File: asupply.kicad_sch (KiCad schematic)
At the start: 108 parts, among them U10 LT3081xDF, U11 LT3042xMSE, U12 LT3045xMSE, U13 LT3045xMSE, U14 LT3042xMSE, U15 LT3094xMSE, U16 LT3042xMSE, U9 LTC3261

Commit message: change diodes
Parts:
- gave numbers to parts that had none: 1
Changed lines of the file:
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@@
   (symbol (lib_id "Device:C") (at 226.06 119.38 0) (unit 1)
     (in_bom yes) (on_board yes)
-    (property "Reference" "C?" (id 0) (at 229.87 121.92 0)
+    (property "Reference" "C193" (id 0) (at 229.87 121.92 0)
       (effects (font (size 1.27 1.27)) (justify left))
     )

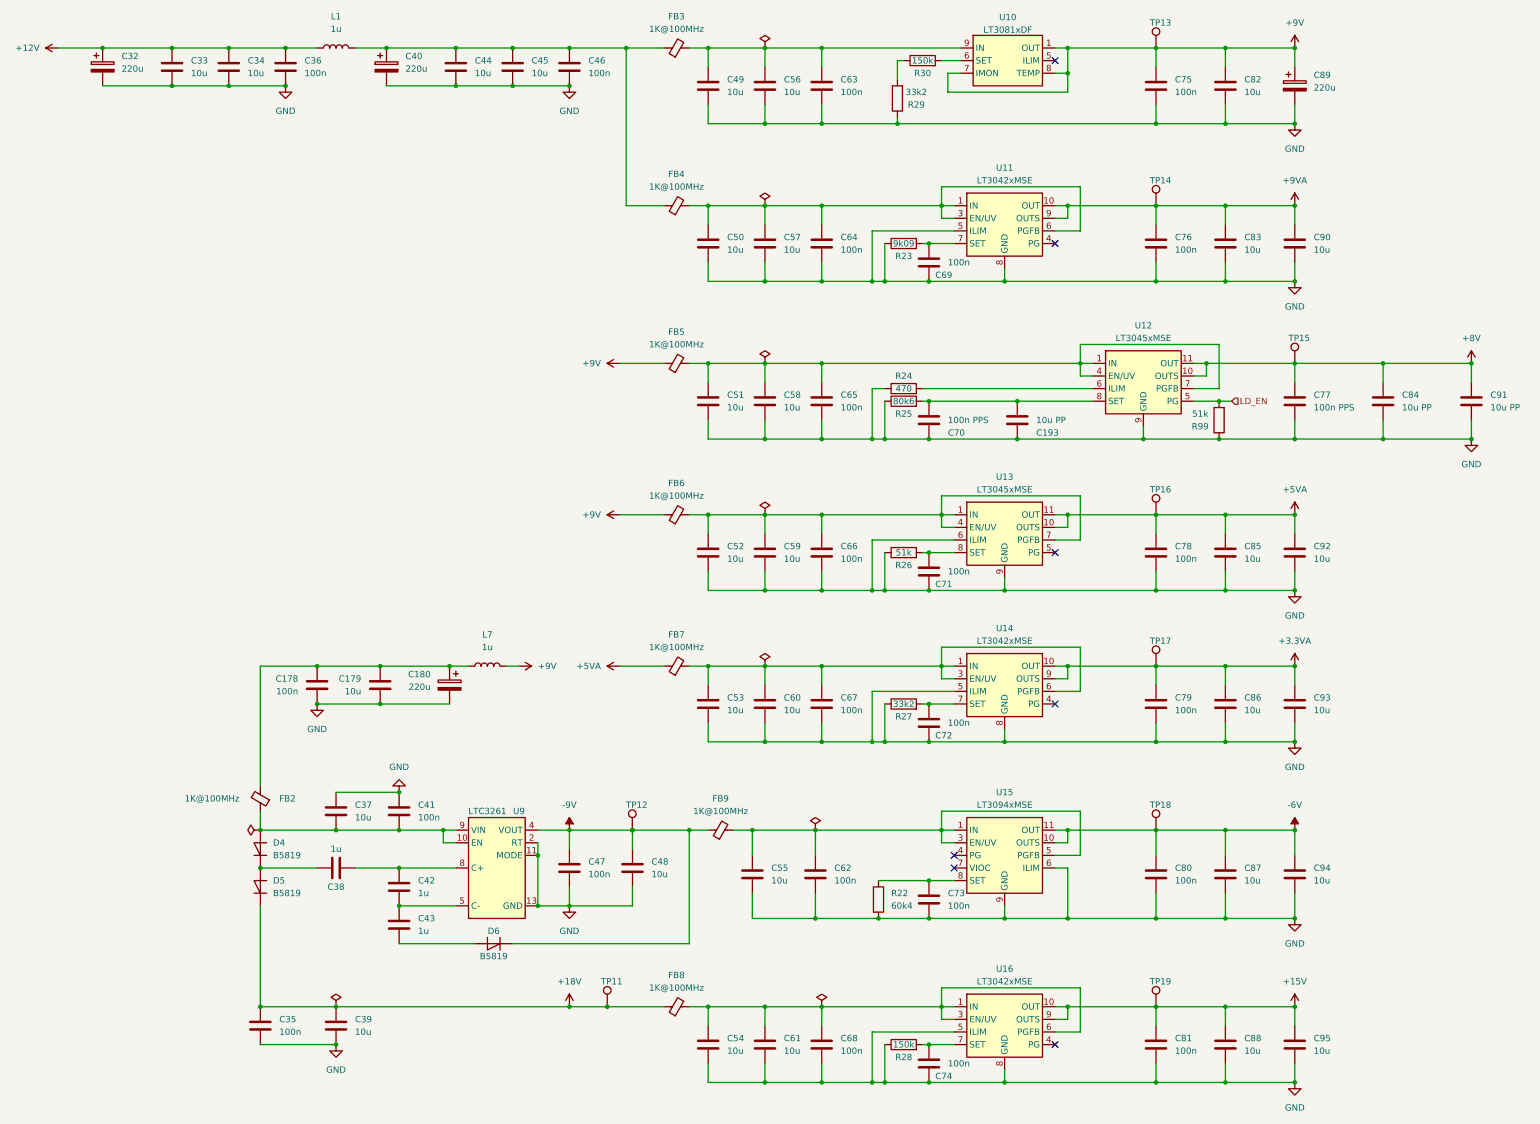
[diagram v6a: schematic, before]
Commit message: import sch to pcb
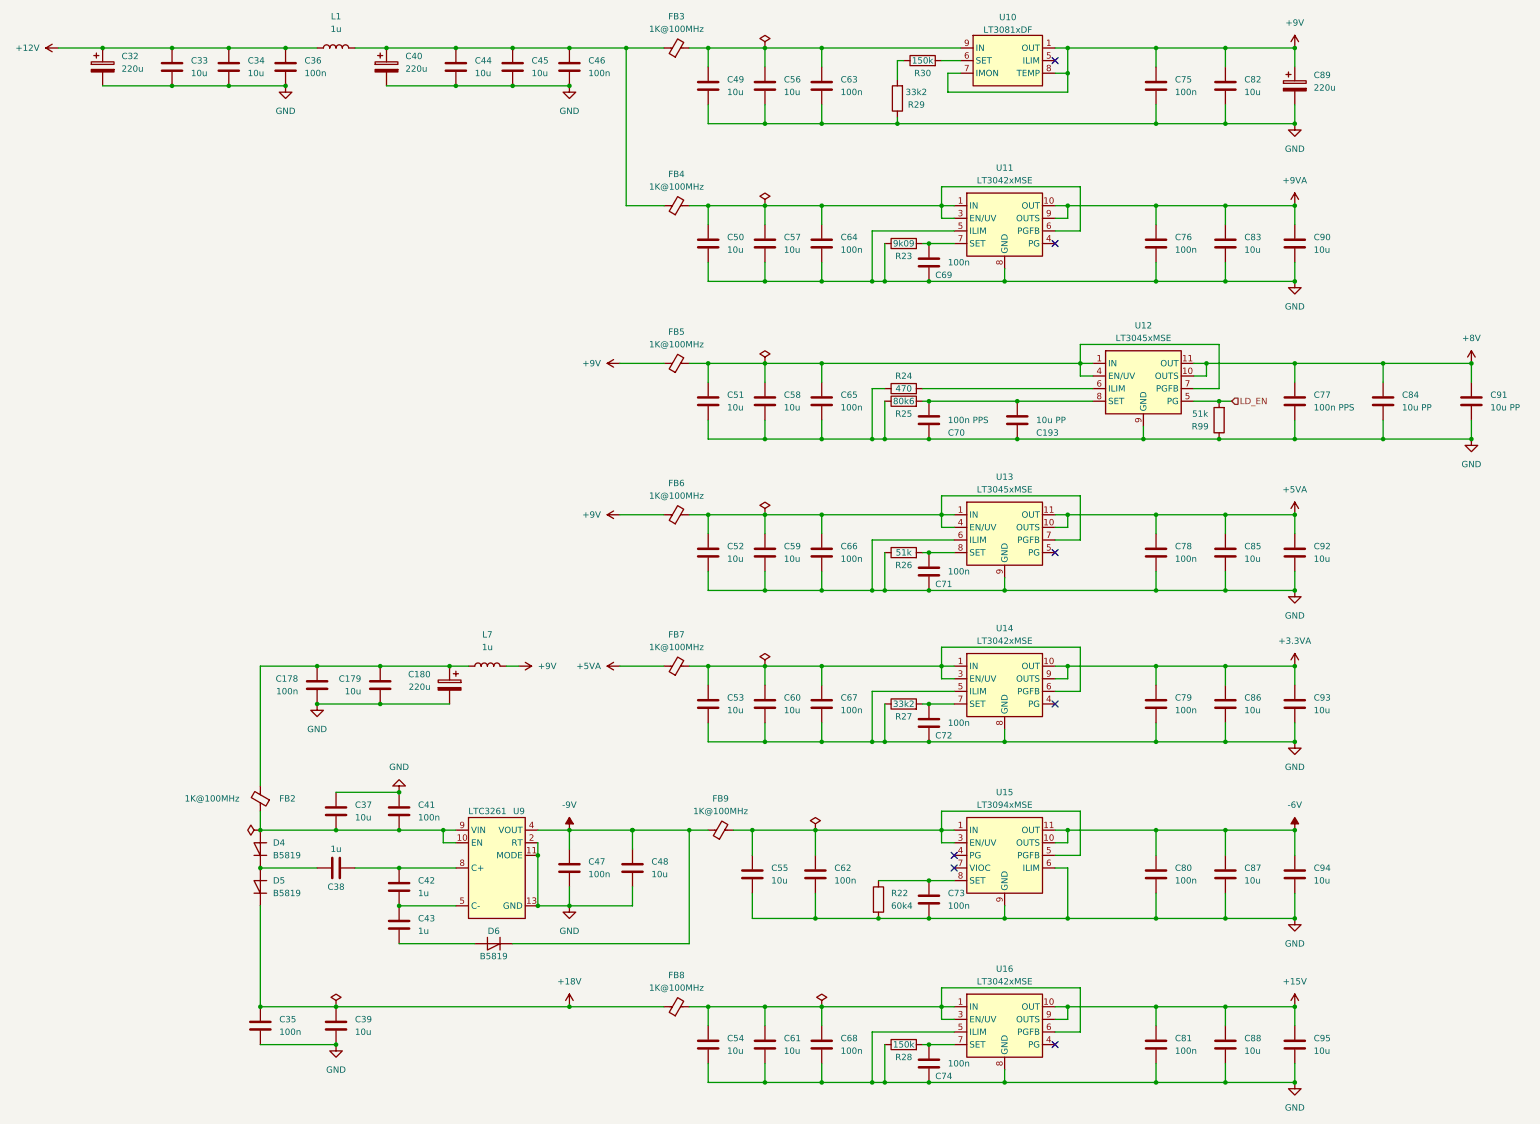
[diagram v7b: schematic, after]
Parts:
- removed TP11, TP12, TP13, TP14, TP15, TP16, TP17, TP18, TP19: TestPoint, TestPoint:TestPoint_Pad_2.0x2.0mm, symbol Connector:TestPoint
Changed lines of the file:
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@@
   (junction (at 254 91.44) (diameter 0) (color 0 0 0 0)
   )
-  (junction (at 143.51 237.49) (diameter 0) (color 0 0 0 0)
-  )
   (junction (at 135.89 237.49) (diameter 0) (color 0 0 0 0)
   )
@@
     (stroke (width 0) (type default) (color 0 0 0 0))
   )
-  (wire (pts (xy 135.89 237.49) (xy 143.51 237.49))
+  (wire (pts (xy 135.89 237.49) (xy 154.94 237.49))
     (stroke (width 0) (type default) (color 0 0 0 0))
   )
@@
     (stroke (width 0) (type default) (color 0 0 0 0))
   )
-  (wire (pts (xy 143.51 237.49) (xy 154.94 237.49))
-    (stroke (width 0) (type default) (color 0 0 0 0))
-  )
   (wire (pts (xy 199.39 91.44) (xy 208.28 91.44))
     (stroke (width 0) (type default) (color 0 0 0 0))
@@
     (pin "2")
   )
-  (symbol (lib_id "Connector:TestPoint") (at 281.94 107.95 0) (unit 1)
-    (in_bom yes) (on_board yes)
-    (property "Reference" "TP15" (id 0) (at 280.67 102.87 0)
-      (effects (font (size 1.27 1.27)) (justify left))
-    )
-    (property "Value" "TestPoint" (id 1) (at 283.337 106.3502 0)
-      (effects (font (size 1.27 1.27)) (justify left) hide)
-    )
-    (property "Footprint" "TestPoint:TestPoint_Pad_2.0x2.0mm" (id 2) (at 287.02 107.95 0)
-      (effects (font (size 1.27 1.27)) hide)
-    )
-    (property "Datasheet" "~" (id 3) (at 287.02 107.95 0)
-      (effects (font (size 1.27 1.27)) hide)
-    )
-    (pin "1")
-  )
   (symbol (lib_id "power:-9V") (at 135.89 201.93 0) (unit 1)
     (in_bom yes) (on_board yes) (fields_autoplaced)
@@
     (pin "2")
   )
-  (symbol (lib_id "Connector:TestPoint") (at 254 168.91 0) (unit 1)
-    (in_bom yes) (on_board yes)
-    (property "Reference" "TP17" (id 0) (at 252.73 163.83 0)
-      (effects (font (size 1.27 1.27)) (justify left))
-    )
-    (property "Value" "TestPoint" (id 1) (at 255.397 167.3102 0)
-      (effects (font (size 1.27 1.27)) (justify left) hide)
-    )
-    (property "Footprint" "TestPoint:TestPoint_Pad_2.0x2.0mm" (id 2) (at 259.08 168.91 0)
-      (effects (font (size 1.27 1.27)) hide)
-    )
-    (property "Datasheet" "~" (id 3) (at 259.08 168.91 0)
-      (effects (font (size 1.27 1.27)) hide)
-    )
-    (pin "1")
-  )
   (symbol (lib_id "Device:C") (at 208.28 119.38 0) (unit 1)
     (in_bom yes) (on_board yes)
@@
     (pin "2")
   )
-  (symbol (lib_id "Connector:TestPoint") (at 254 138.43 0) (unit 1)
-    (in_bom yes) (on_board yes)
-    (property "Reference" "TP16" (id 0) (at 252.73 133.35 0)
-      (effects (font (size 1.27 1.27)) (justify left))
-    )
-    (property "Value" "TestPoint" (id 1) (at 255.397 136.8302 0)
-      (effects (font (size 1.27 1.27)) (justify left) hide)
-    )
-    (property "Footprint" "TestPoint:TestPoint_Pad_2.0x2.0mm" (id 2) (at 259.08 138.43 0)
-      (effects (font (size 1.27 1.27)) hide)
-    )
-    (property "Datasheet" "~" (id 3) (at 259.08 138.43 0)
-      (effects (font (size 1.27 1.27)) hide)
-    )
-    (pin "1")
-  )
   (symbol (lib_id "Device:C") (at 281.94 115.57 0) (unit 1)
     (in_bom yes) (on_board yes) (fields_autoplaced)
@@
     (pin "1")
   )
-  (symbol (lib_id "Connector:TestPoint") (at 254 201.93 0) (unit 1)
-    (in_bom yes) (on_board yes)
-    (property "Reference" "TP18" (id 0) (at 252.73 196.85 0)
-      (effects (font (size 1.27 1.27)) (justify left))
-    )
-    (property "Value" "TestPoint" (id 1) (at 255.397 200.3302 0)
-      (effects (font (size 1.27 1.27)) (justify left) hide)
-    )
-    (property "Footprint" "TestPoint:TestPoint_Pad_2.0x2.0mm" (id 2) (at 259.08 201.93 0)
-      (effects (font (size 1.27 1.27)) hide)
-    )
-    (property "Datasheet" "~" (id 3) (at 259.08 201.93 0)
-      (effects (font (size 1.27 1.27)) hide)
-    )
-    (pin "1")
-  )
-  (symbol (lib_id "Connector:TestPoint") (at 254 237.49 0) (unit 1)
-    (in_bom yes) (on_board yes)
-    (property "Reference" "TP19" (id 0) (at 252.73 232.41 0)
-      (effects (font (size 1.27 1.27)) (justify left))
-    )
-    (property "Value" "TestPoint" (id 1) (at 255.397 235.8902 0)
-      (effects (font (size 1.27 1.27)) (justify left) hide)
-    )
-    (property "Footprint" "TestPoint:TestPoint_Pad_2.0x2.0mm" (id 2) (at 259.08 237.49 0)
-      (effects (font (size 1.27 1.27)) hide)
-    )
-    (property "Datasheet" "~" (id 3) (at 259.08 237.49 0)
-      (effects (font (size 1.27 1.27)) hide)
-    )
-    (pin "1")
-  )
   (symbol (lib_id "power:PWR_FLAG") (at 73.66 201.93 90) (unit 1)
     (in_bom yes) (on_board yes) (fields_autoplaced)
@@
     (pin "1")
   )
-  (symbol (lib_id "Connector:TestPoint") (at 148.556 201.93 0) (unit 1)
-    (in_bom yes) (on_board yes)
-    (property "Reference" "TP12" (id 0) (at 147.286 196.85 0)
-      (effects (font (size 1.27 1.27)) (justify left))
-    )
-    (property "Value" "TestPoint" (id 1) (at 149.953 200.3302 0)
-      (effects (font (size 1.27 1.27)) (justify left) hide)
-    )
-    (property "Footprint" "TestPoint:TestPoint_Pad_2.0x2.0mm" (id 2) (at 153.636 201.93 0)
-      (effects (font (size 1.27 1.27)) hide)
-    )
-    (property "Datasheet" "~" (id 3) (at 153.636 201.93 0)
-      (effects (font (size 1.27 1.27)) hide)
-    )
-    (pin "1")
-  )
   (symbol (lib_id "Device:C") (at 267.97 245.11 0) (unit 1)
     (in_bom yes) (on_board yes) (fields_autoplaced)
@@
     (pin "1")
   )
-  (symbol (lib_id "Connector:TestPoint") (at 254 44.45 0) (unit 1)
-    (in_bom yes) (on_board yes)
-    (property "Reference" "TP13" (id 0) (at 252.73 39.37 0)
-      (effects (font (size 1.27 1.27)) (justify left))
-    )
-    (property "Value" "TestPoint" (id 1) (at 255.397 42.8502 0)
-      (effects (font (size 1.27 1.27)) (justify left) hide)
-    )
-    (property "Footprint" "TestPoint:TestPoint_Pad_2.0x2.0mm" (id 2) (at 259.08 44.45 0)
-      (effects (font (size 1.27 1.27)) hide)
-    )
-    (property "Datasheet" "~" (id 3) (at 259.08 44.45 0)
-      (effects (font (size 1.27 1.27)) hide)
-    )
-    (pin "1")
-  )
   (symbol (lib_id "Device:D_Shockley") (at 120.65 224.79 180) (unit 1)
     (in_bom yes) (on_board yes)
@@
     (pin "2")
   )
-  (symbol (lib_id "Connector:TestPoint") (at 254 76.2 0) (unit 1)
-    (in_bom yes) (on_board yes)
-    (property "Reference" "TP14" (id 0) (at 252.73 71.12 0)
-      (effects (font (size 1.27 1.27)) (justify left))
-    )
-    (property "Value" "TestPoint" (id 1) (at 255.397 74.6002 0)
-      (effects (font (size 1.27 1.27)) (justify left) hide)
-    )
-    (property "Footprint" "TestPoint:TestPoint_Pad_2.0x2.0mm" (id 2) (at 259.08 76.2 0)
-      (effects (font (size 1.27 1.27)) hide)
-    )
-    (property "Datasheet" "~" (id 3) (at 259.08 76.2 0)
-      (effects (font (size 1.27 1.27)) hide)
-    )
-    (pin "1")
-  )
   (symbol (lib_id "Device:C") (at 135.89 209.55 0) (unit 1)
     (in_bom yes) (on_board yes) (fields_autoplaced)
@@
       (effects (font (size 1.27 1.27)) hide)
     )
-    (pin "1")
-  )
-  (symbol (lib_id "Connector:TestPoint") (at 143.51 237.49 0) (unit 1)
-    (in_bom yes) (on_board yes)
-    (property "Reference" "TP11" (id 0) (at 142.24 232.41 0)
-      (effects (font (size 1.27 1.27)) (justify left))
-    )
-    (property "Value" "TestPoint" (id 1) (at 144.907 235.8902 0)
-      (effects (font (size 1.27 1.27)) (justify left) hide)
-    )
-    (property "Footprint" "TestPoint:TestPoint_Pad_2.0x2.0mm" (id 2) (at 148.59 237.49 0)
-      (effects (font (size 1.27 1.27)) hide)
-    )
-    (property "Datasheet" "~" (id 3) (at 148.59 237.49 0)
-      (effects (font (size 1.27 1.27)) hide)
-    )

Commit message: sync
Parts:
- removed C193: 10u PP, Capacitor_SMD:C_1812_4532Metric, symbol Device:C
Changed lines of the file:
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@@
   (junction (at 186.69 76.2) (diameter 0) (color 0 0 0 0)
   )
-  (junction (at 226.06 123.19) (diameter 0) (color 0 0 0 0)
-  )
   (junction (at 198.12 219.71) (diameter 0) (color 0 0 0 0)
   )
@@
   (junction (at 88.9 201.93) (diameter 0) (color 0 0 0 0)
   )
-  (junction (at 226.06 115.57) (diameter 0) (color 0 0 0 0)
-  )
   (junction (at 254 201.93) (diameter 0) (color 0 0 0 0)
   )
@@
     (stroke (width 0) (type default) (color 0 0 0 0))
   )
-  (wire (pts (xy 208.28 115.57) (xy 226.06 115.57))
+  (wire (pts (xy 208.28 115.57) (xy 241.3 115.57))
     (stroke (width 0) (type default) (color 0 0 0 0))
   )
@@
     (stroke (width 0) (type default) (color 0 0 0 0))
   )
-  (wire (pts (xy 226.06 123.19) (xy 251.46 123.19))
-    (stroke (width 0) (type default) (color 0 0 0 0))
-  )
   (wire (pts (xy 199.39 146.05) (xy 199.39 153.67))
     (stroke (width 0) (type default) (color 0 0 0 0))
@@
     (stroke (width 0) (type default) (color 0 0 0 0))
   )
-  (wire (pts (xy 208.28 123.19) (xy 226.06 123.19))
+  (wire (pts (xy 208.28 123.19) (xy 251.46 123.19))
     (stroke (width 0) (type default) (color 0 0 0 0))
   )
@@
     (stroke (width 0) (type default) (color 0 0 0 0))
   )
-  (wire (pts (xy 226.06 115.57) (xy 241.3 115.57))
-    (stroke (width 0) (type default) (color 0 0 0 0))
-  )
   (wire (pts (xy 163.83 123.19) (xy 163.83 119.38))
     (stroke (width 0) (type default) (color 0 0 0 0))
@@
       (effects (font (size 1.27 1.27)) hide)
     )
-    (pin "1")
-    (pin "2")
-  )
-  (symbol (lib_id "Device:C") (at 226.06 119.38 0) (unit 1)
-    (in_bom yes) (on_board yes)
-    (property "Reference" "C193" (id 0) (at 229.87 121.92 0)
-      (effects (font (size 1.27 1.27)) (justify left))
-    )
-    (property "Value" "10u PP" (id 1) (at 229.87 119.38 0)
-      (effects (font (size 1.27 1.27)) (justify left))
-    )
-    (property "Footprint" "Capacitor_SMD:C_1812_4532Metric" (id 2) (at 227.0252 123.19 0)
-      (effects (font (size 1.27 1.27)) hide)
-    )
-    (property "Datasheet" "~" (id 3) (at 226.06 119.38 0)
-      (effects (font (size 1.27 1.27)) hide)
-    )
-    (property "MFR_PN" "16MU106MC44532" (id 4) (at 226.06 119.38 0)
-      (effects (font (size 1.27 1.27)) hide)
-    )
